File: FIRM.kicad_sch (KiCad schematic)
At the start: 94 parts, among them J2 Conn_01x02_Pin, Q1 IRLML6402, U1 W25N04KVZEIR, U10 STM32F446ZCHx, U2 STM32H743VIHx, U3 ADXL371, U5 INA219AxDCN, U6 MIC5219-3.3YM5, U9 A-USBC-20F0-EA-GSR05, Y1 25 MHz, Y2 25 MHz

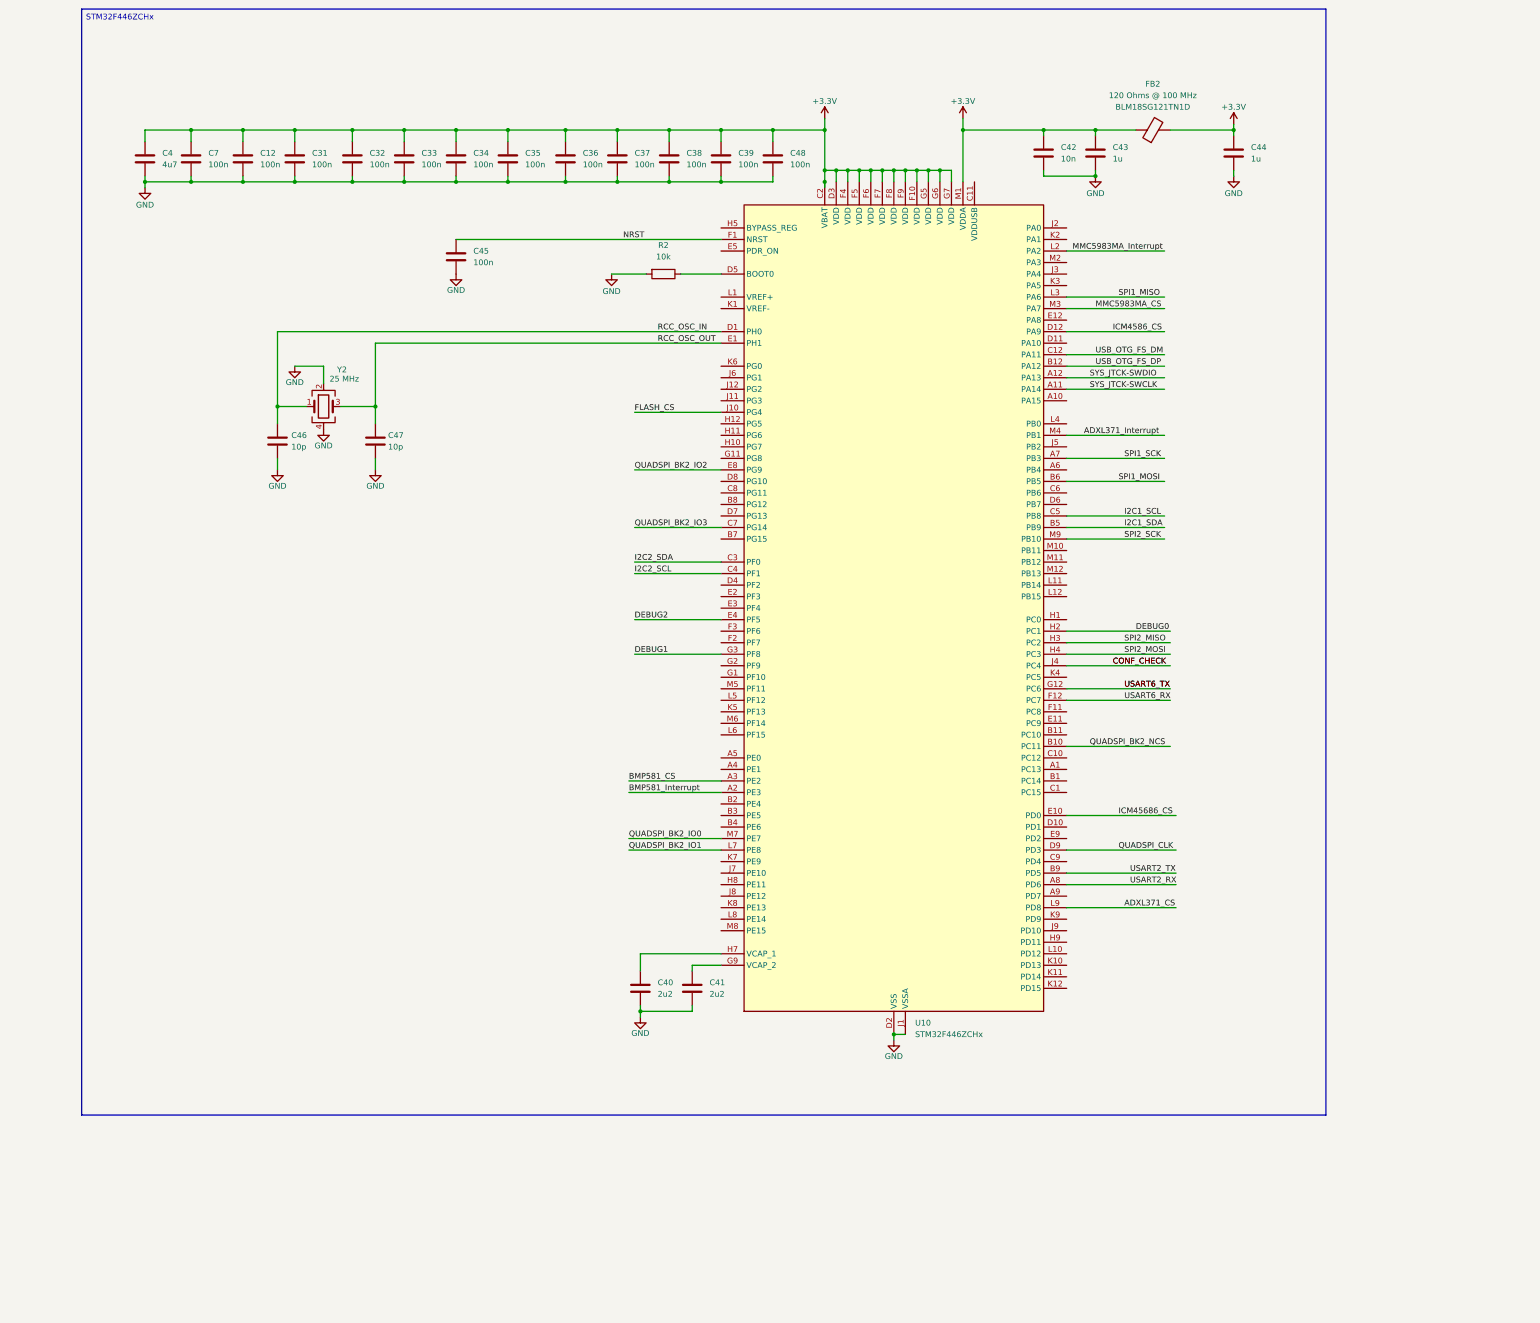
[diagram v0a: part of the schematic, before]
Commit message: Updated STM names
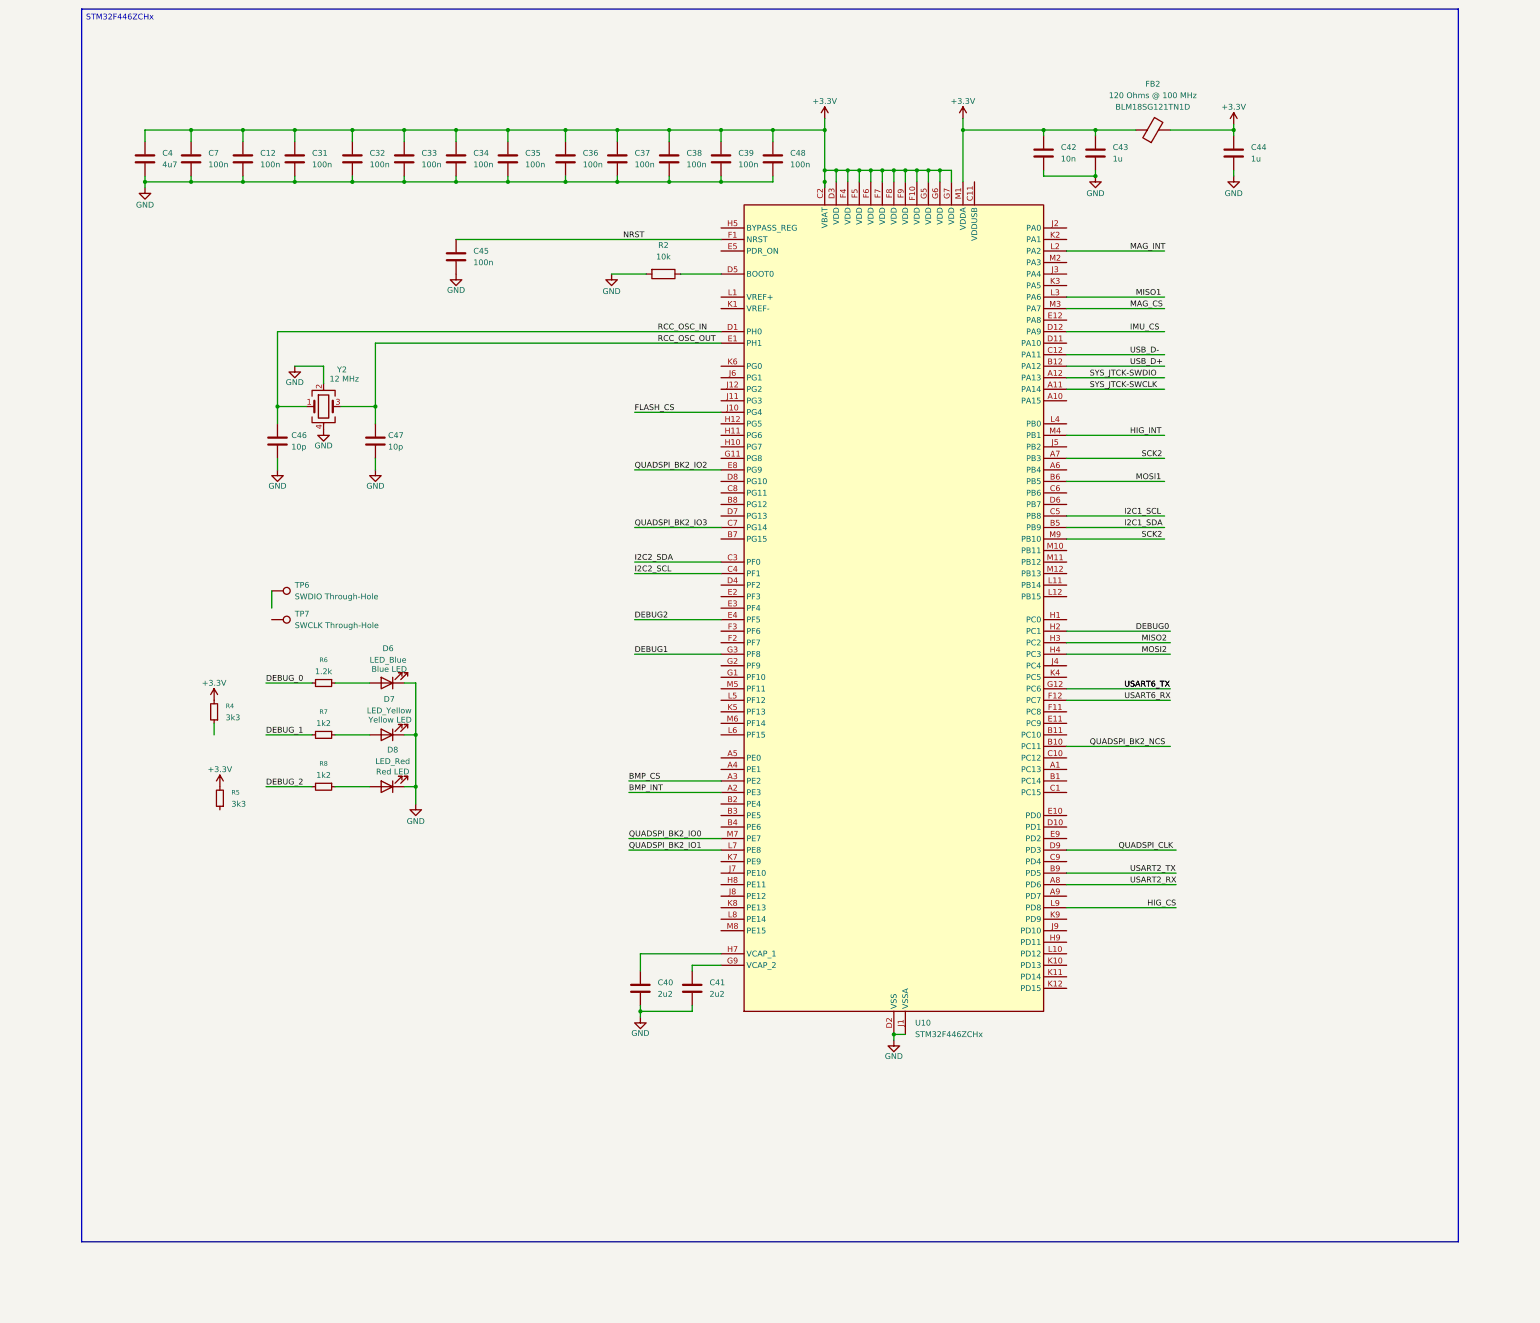
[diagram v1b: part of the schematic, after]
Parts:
- added D6: LED_Blue, LED_SMD:LED_0402_1005Metric, symbol Device:LED
- added D7: LED_Yellow, LED_SMD:LED_0402_1005Metric, symbol Device:LED
- added D8: LED_Red, LED_SMD:LED_0402_1005Metric, symbol Device:LED
- added R4, R5: 3k3, Resistor_SMD:R_0402_1005Metric, symbol Device:R_Small
- added R6: 1.2k, Resistor_SMD:R_0402_1005Metric, symbol Device:R_Small
- added R7, R8: 1k2, Resistor_SMD:R_0402_1005Metric, symbol Device:R_Small
- added TP6: SWDIO Through-Hole, connectors:Testpoint_1.5x1.5mm_1.0mm, symbol Connector:TestPoint
- added TP7: SWCLK Through-Hole, connectors:Testpoint_1.5x1.5mm_1.0mm, symbol Connector:TestPoint
- Y2: value 25 MHz -> 12 MHz
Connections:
- net ADXL371_CS is gone; now on net HIG_CS: U10.L9 (PD8)
- net ADXL371_Interrupt is gone; now on net HIG_INT: U10.M4 (PB1)
- net BMP581_CS is gone; now on net BMP_CS: U10.A3 (PE2)
- net BMP581_Interrupt is gone; now on net BMP_INT: U10.A2 (PE3)
- net ICM4586_CS is gone; now on net IMU_CS: U10.D12 (PA9)
- net MMC5983MA_CS is gone; now on net MAG_CS: U10.M3 (PA7)
- net MMC5983MA_Interrupt is gone; now on net MAG_INT: U10.L2 (PA2)
- net SPI2_MISO is gone; now on net MISO2: U10.H3 (PC2)
- net SPI2_MOSI is gone; now on net MOSI2: U10.H4 (PC3)
- net SPI2_SCK is gone; now on net SCK2: U10.M9 (PB10)
- net USB_OTG_FS_DM is gone; now on net USB_D-: U10.C12 (PA11)
- net USB_OTG_FS_DP is gone; now on net USB_D+: U10.B12 (PA12)
- net +3.3V: now also R4.2, R5.2
- net GND: now also D6.1 (K), D7.1 (K), D8.1 (K)
- net SCK2: now also U10.A7 (PB3)
- net SPI1_MISO: no longer U10.L3 (PA6)
- net SPI1_SCK: no longer U10.A7 (PB3)
- net CONF_CHECK: no longer names the net of U10.J4 (PC4)
- net ICM45686_CS: no longer names the net of U10.E10 (PD0)
- net SPI1_MOSI renamed MOSI1
- new net: D6.2 (A), R6.1
- new net: D7.2 (A), R7.1
- new net: D8.2 (A), R8.1
- new net: U3.10 (RES), U3.13 (GND), U3.16 (GND)
- new net DEBUG_0: R6.2
- new net DEBUG_1: R7.2
- new net DEBUG_2: R8.2
- new net MISO1: U10.L3 (PA6)

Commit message: Started adding Pins From Shoe
Started added pins from shoe, unsure about global variable and connection based on previous schematic.
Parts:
- added +3.3V: +3.3V Test Point, connectors:Testpoint_1.5x1.5mm_1.0mm, symbol Connector:TestPoint
- added GND: GND Test Point, connectors:Testpoint_1.5x1.5mm_1.0mm, symbol Connector:TestPoint
- added SPI_MISO: MISO Test Point, connectors:Testpoint_1.5x1.5mm_1.0mm, symbol Connector:TestPoint
- added SPI_MOSI: MOSI Test Point, connectors:Testpoint_1.5x1.5mm_1.0mm, symbol Connector:TestPoint
- added TP9: PA2 Test Point, connectors:Testpoint_1.5x1.5mm_1.0mm, symbol Connector:TestPoint
- added UART_RX: UART RX Test Point, connectors:Testpoint_1.5x1.5mm_1.0mm, symbol Connector:TestPoint
- added UART_RX: UART TX, connectors:Testpoint_1.5x1.5mm_1.0mm, symbol Connector:TestPoint
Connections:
- net +3.3V: now also +3.3V.1
- net GND: now also GND.1
- new net: U3.10 (RES), U3.13 (GND), U3.16 (GND)
- new net SPI_MISO: SPI_MISO.1
- new net SPI_MOSI: SPI_MOSI.1
- new net UART_RX: UART_RX.1
- new net UART_TX: UART_RX.1
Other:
- note added: "idk if im doing this right yikes"
- moved on the sheet: C12, C31, C32, C33, C34, C35, C36, C37, C38, C39, C4, C40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

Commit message: Update test pins
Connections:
- net at TP9.1: no longer names the net of TP9.1
- new net: U3.10 (RES), U3.13 (GND), U3.16 (GND)
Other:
- note removed: "idk if im doing this right yikes"
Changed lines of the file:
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@@
 		)
 	)
-	(text "idk if im doing this right yikes\n"
-		(exclude_from_sim no)
-		(at 251.714 262.89 0)
-		(effects
-			(font
-				(size 1.27 1.27)
-			)
-		)
-	)
 	(text "INA219AIDCNR Voltage Sensor\n"
 		(exclude_from_sim no)
@@
 			(effects
 				(font
-					(size 1.27 1.27)
-				)
-				(justify left)
-				(hide yes)
-			)
-		)
-	)
-	(global_label ""
-		(shape input)
-		(at 220.98 306.07 0)
-		(fields_autoplaced yes)
-		(effects
-			(font
-				(size 1.27 1.27)
-			)
-			(justify left)
-		)
-		(property "Intersheetrefs" "${INTERSHEET_REFS}"
-			(at 224.2192 306.07 0)
-			(effects
-				(font

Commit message: Updated testpoints
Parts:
- removed +3.3V: +3.3V Test Point, connectors:Testpoint_1.5x1.5mm_1.0mm, symbol Connector:TestPoint
- removed GND: GND Test Point, connectors:Testpoint_1.5x1.5mm_1.0mm, symbol Connector:TestPoint
- removed SPI_MISO: MISO Test Point, connectors:Testpoint_1.5x1.5mm_1.0mm, symbol Connector:TestPoint
- removed SPI_MOSI: MOSI Test Point, connectors:Testpoint_1.5x1.5mm_1.0mm, symbol Connector:TestPoint
- removed TP9: PA2 Test Point, connectors:Testpoint_1.5x1.5mm_1.0mm, symbol Connector:TestPoint
- removed UART_RX: UART RX Test Point, connectors:Testpoint_1.5x1.5mm_1.0mm, symbol Connector:TestPoint
- removed UART_RX: UART TX, connectors:Testpoint_1.5x1.5mm_1.0mm, symbol Connector:TestPoint
- added TP1: 3.3V Test Point, connectors:Testpoint_1.5x1.5mm_1.0mm, symbol Connector:TestPoint
- added TP12: ARM_2 Test Point, connectors:Testpoint_1.5x1.5mm_1.0mm, symbol Connector:TestPoint
- added TP13: SENS_A Test Point, connectors:Testpoint_1.5x1.5mm_1.0mm, symbol Connector:TestPoint
- added TP15: BUSY Test Point, connectors:Testpoint_1.5x1.5mm_1.0mm, symbol Connector:TestPoint
- added TP16: MISO Test Point, connectors:Testpoint_1.5x1.5mm_1.0mm, symbol Connector:TestPoint
- added TP17: MOSI Test Point, connectors:Testpoint_1.5x1.5mm_1.0mm, symbol Connector:TestPoint
- added TP18: NSS Test Point, connectors:Testpoint_1.5x1.5mm_1.0mm, symbol Connector:TestPoint
- added TP19: SCK Test Point, connectors:Testpoint_1.5x1.5mm_1.0mm, symbol Connector:TestPoint
- added TP2: GND Test Point, connectors:Testpoint_1.5x1.5mm_1.0mm, symbol Connector:TestPoint
- added TP20: RXEN Test Point, connectors:Testpoint_1.5x1.5mm_1.0mm, symbol Connector:TestPoint
- added TP21: TXEN Test Point, connectors:Testpoint_1.5x1.5mm_1.0mm, symbol Connector:TestPoint
- added TP3: UART_RX Test Point, connectors:Testpoint_1.5x1.5mm_1.0mm, symbol Connector:TestPoint
- added TP4: UART_TX Test Point, connectors:Testpoint_1.5x1.5mm_1.0mm, symbol Connector:TestPoint
- added TP5: SPI_MISO Test Point, connectors:Testpoint_1.5x1.5mm_1.0mm, symbol Connector:TestPoint
- added TP6: SPI_MOSI Test Point, connectors:Testpoint_1.5x1.5mm_1.0mm, symbol Connector:TestPoint
- TP10: renamed from TP4; value PA9 Test Point -> FIRE_B Test Point
- TP11: renamed from TP5; value PA10 Test Point -> ARM_1 Test Point
- TP14: value 3.3V Test Point -> SENS_B Test Point
- TP7: renamed from TP1; value PA0 Test Point -> SPI_SCK Test Point
- TP8: renamed from TP2; value PA1 Test Point -> VBAT Test Point
- TP9: renamed from TP3; value PA2 Test Point -> FIRE_A Test Point
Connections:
- net PA1 is gone; now on net VBAT: TP8.1
- net +3.3V: now also TP1.1; no longer TP14.1
- net GND: now also TP2.1
- net SPI_MISO: now also TP5.1
- net SPI_MOSI: now also TP6.1
- net UART_RX: now also TP3.1
- net UART_TX: now also TP4.1
- net PA0 renamed SPI_SCK
- net PA10 renamed ARM_1
- net PA2 renamed FIRE_A
- net PA9 renamed FIRE_B
- new net: U3.10 (RES), U3.13 (GND), U3.16 (GND)
- new net ARM_2: TP12.1
- new net BUSY: TP15.1
- new net MISO: TP16.1
- new net MOSI: TP17.1
- new net NSS: TP18.1
- new net RXEN: TP20.1
- new net SCK: TP19.1
- new net SENS_A: TP13.1
- new net SENS_B: TP14.1
- new net TXEN: TP21.1
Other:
- moved on the sheet: TP10, TP11, TP7, TP8, TP9

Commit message: Updated Testpoints
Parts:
- removed TP16: MISO Test Point, connectors:Testpoint_1.5x1.5mm_1.0mm, symbol Connector:TestPoint
- removed TP17: MOSI Test Point, connectors:Testpoint_1.5x1.5mm_1.0mm, symbol Connector:TestPoint
- removed TP19: SCK Test Point, connectors:Testpoint_1.5x1.5mm_1.0mm, symbol Connector:TestPoint
- renumbered TP18 to TP16, TP20 to TP18, TP21 to TP19
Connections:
- net SPI_MISO is gone; now on net MISO1: TP5.1
- net SPI_MOSI is gone; now on net MOSI1: TP6.1
- net UART_RX is gone; now on net USART2_RX: TP3.1
- net UART_TX is gone; now on net USART2_TX: TP4.1
- net ARM_1: now also U10.J12 (PG2)
- net ARM_2: now also U10.J11 (PG3)
- net BUSY: now also U10.H10 (PG7)
- net FIRE_A: now also U10.K6 (PG0)
- net FIRE_B: now also U10.J6 (PG1)
- net NSS: now also U10.G11 (PG8)
- net RXEN: now also U10.D8 (PG10)
- net SCK2: no longer U10.A7 (PB3)
- net SENS_A: now also U10.H12 (PG5)
- net SENS_B: now also U10.H11 (PG6)
- net TXEN: now also U10.C8 (PG11)
- net SPI_SCK renamed SCK1
- net SCK1: now also U10.A7 (PB3)
- new net: U3.10 (RES), U3.13 (GND), U3.16 (GND)
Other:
- moved on the sheet: TP16, TP18, TP19
